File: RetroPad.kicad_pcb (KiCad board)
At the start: 2 copper layers, 125 x 45 mm, 13 parts, among them J1 DB9_Female

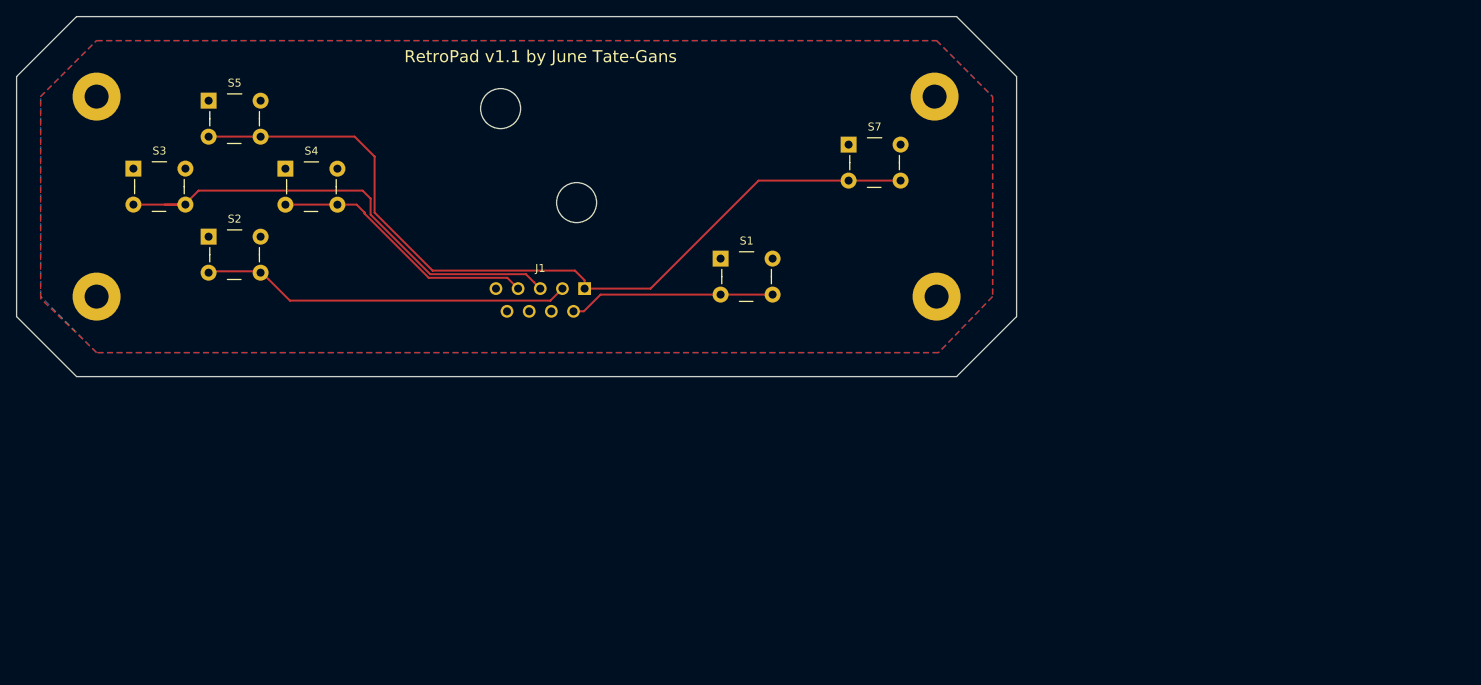
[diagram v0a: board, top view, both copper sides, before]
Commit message: pcb: Major revision to mechanicals
This is a near total redesign of the RetroPad. Electrically it should be
identical, aside from two additional buttons. Major features planned are:

  - Two additional fire buttons using POTX and POTY for games that support it.
  - Migrates from raw-through hole wiring to a proper male 9-pin D-Sub
    connector. This should be significantly more robust.
  - Mechanical redesign of the positioning for the buttons and D-pad.
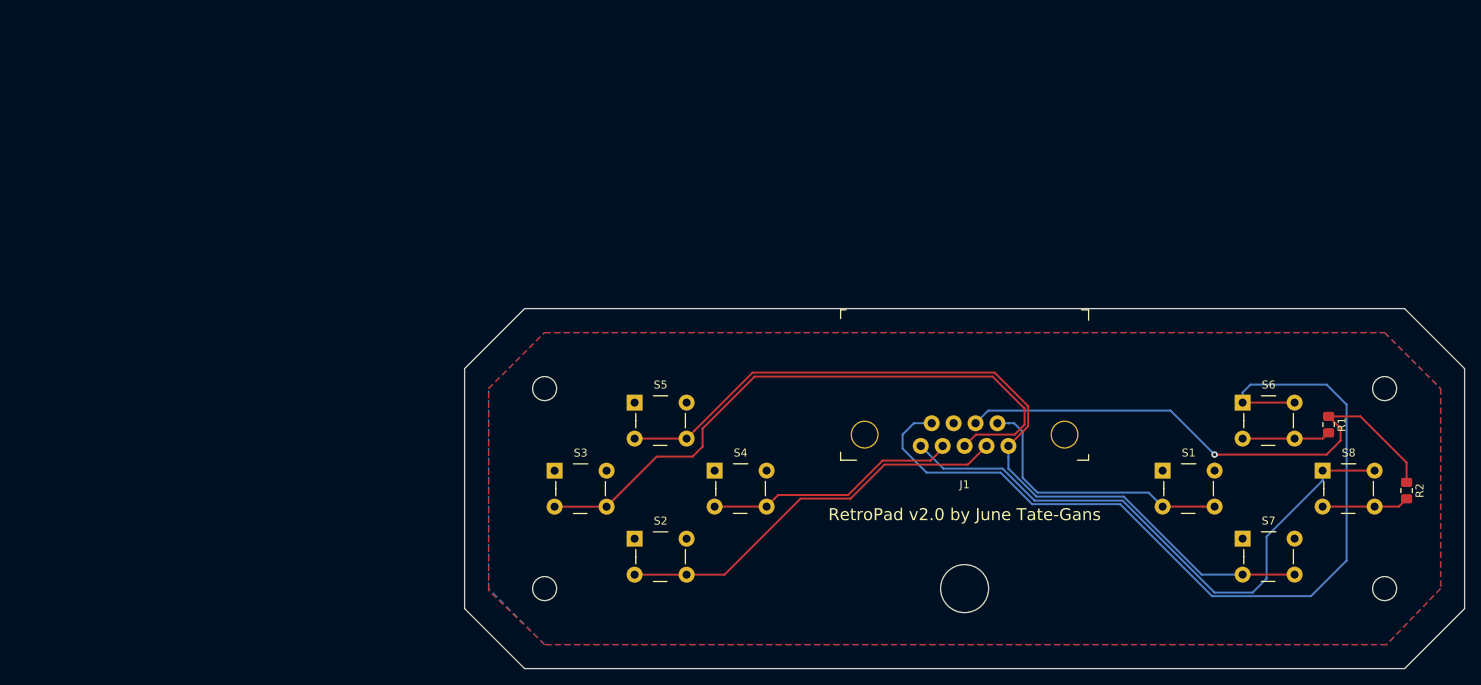
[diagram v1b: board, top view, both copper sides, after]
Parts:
- removed ? (x4): , MountingHole:MountingHole_3mm_Pad
- removed ? (x2): , MountingHole:MountingHole_5mm
- added 3mm_LL: MountingHole_3mm, MountingHole:MountingHole_3mm, F.Cu at (106.0, 111.5)
- added 3mm_LR: MountingHole_3mm, MountingHole:MountingHole_3mm, F.Cu at (211.0, 111.5)
- added 3mm_UL: MountingHole_3mm, MountingHole:MountingHole_3mm, F.Cu at (106.0, 86.5)
- added 3mm_UR: MountingHole_3mm, MountingHole:MountingHole_3mm, F.Cu at (211.0, 86.5)
- added 6mm_C: MountingHole_6mm, MountingHole:MountingHole_6mm, F.Cu at (158.5, 111.5)
- added R1: 330, Resistor_SMD:R_0805_2012Metric_Pad1.15x1.40mm_HandSolder, F.Cu at (204.0, 91.0)
- added R2: 330, Resistor_SMD:R_0805_2012Metric_Pad1.15x1.40mm_HandSolder, F.Cu at (213.8, 99.2)
- added S6: FIRE2, digikey-footprints:Switch_Tactile_THT_B3F-1xxx, F.Cu at (193.2, 88.2)
- added S8: FIRE3, digikey-footprints:Switch_Tactile_THT_B3F-1xxx, F.Cu at (203.2, 96.7)
- J1: value DB9_Female -> 5747840-3; footprint Connector_Dsub:DSUB-9-Pads -> digikey-footprints:DSUB-9_Jack_5747840-3
- moved S7 69.7 mm to (193.2, 105.2)
- moved S4 65.6 mm to (127.2, 96.7)
- moved S2 65.3 mm to (117.2, 105.2)
- moved S5 65.3 mm to (117.2, 88.2)
- moved S3 64.8 mm to (107.2, 96.8)
- moved S1 61.3 mm to (183.2, 96.7)
- moved J1 50.9 mm to (158.5, 92.2)
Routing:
- net /POTX: track 0.00 -> 112.9 mm
- net /POTY: track 0.00 -> 74.4 mm
- net /5V: track 0.00 -> 67.6 mm, vias 0 -> 1
- net /LEFT: track 60.4 -> 79.1 mm
- net Net-(R1-Pad2): track 0.00 -> 11.1 mm
- net Net-(R2-Pad2): track 0.00 -> 10.9 mm
- net /FIRE: track 25.8 -> 34.8 mm
- net /DOWN: track 46.4 -> 50.7 mm
- net /RIGHT: track 33.5 -> 31.8 mm
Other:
- board text added: "Open Source Hardware"
- board text added: "RetroPad v2.0 by June Tate-Gans"
- board text added: "http://github.com/jtgans/RetroPad"
- board text removed: "RetroPad v1.1 by June Tate-Gans"
